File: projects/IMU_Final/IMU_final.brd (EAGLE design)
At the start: 54.6 x 22.5 mm, 6 parts, among them IC1 ISM330DHCXTR, J1 19428-0004

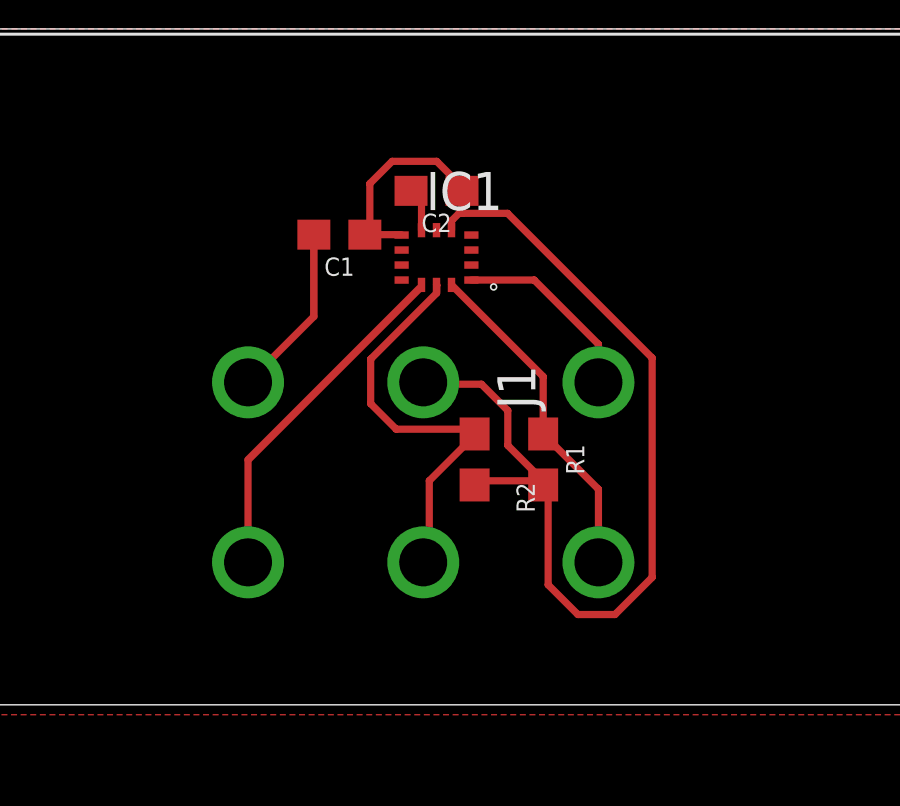
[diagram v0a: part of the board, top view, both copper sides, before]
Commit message: Final IMU Schematic
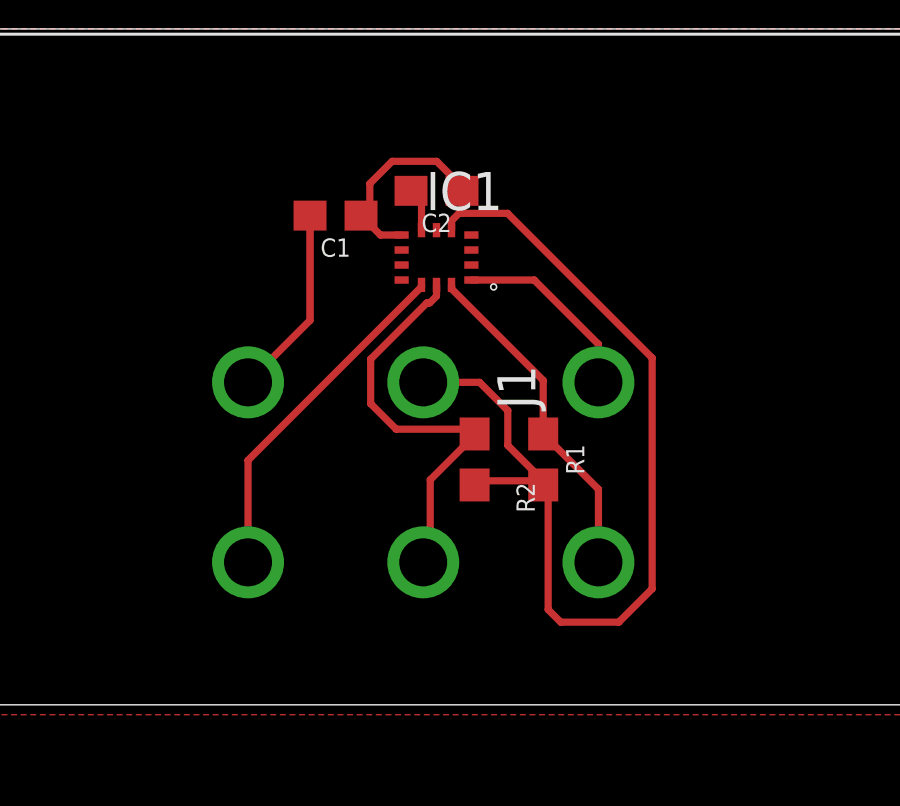
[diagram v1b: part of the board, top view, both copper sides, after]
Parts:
- moved C1 0.65 mm to (-1.14, 21.7)
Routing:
- net 3V3: track 40.1 -> 41.1 mm
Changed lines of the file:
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@@
 </autorouter>
 <elements>
-<element name="C1" library="SparkFun-Capacitors" package="0603" value="0.1uF" x="-1.016" y="21.082" smashed="yes" rot="R180">
-<attribute name="NAME" x="-1.016" y="20.32" size="0.6096" layer="25" font="vector" ratio="20" rot="R180" align="bottom-center"/>
-<attribute name="PROD_ID" value="CAP-00810" x="-16.256" y="56.642" size="1.778" layer="27" rot="R180" display="off"/>
-<attribute name="VALUE" x="-1.016" y="21.844" size="0.6096" layer="27" font="vector" ratio="20" rot="R180" align="top-center"/>
+<element name="C1" library="SparkFun-Capacitors" package="0603" value="0.1uF" x="-1.143" y="21.717" smashed="yes" rot="R180">
+<attribute name="NAME" x="-1.143" y="20.955" size="0.6096" layer="25" font="vector" ratio="20" rot="R180" align="bottom-center"/>
+<attribute name="PROD_ID" value="CAP-00810" x="-16.383" y="57.277" size="1.778" layer="27" rot="R180" display="off"/>
+<attribute name="VALUE" x="-1.143" y="22.479" size="0.6096" layer="27" font="vector" ratio="20" rot="R180" align="top-center"/>
 </element>
 <element name="C2" library="SparkFun-Capacitors" package="0603" value="0.1uF" x="2.2225" y="22.5425" smashed="yes" rot="R180">
@@
 <contactref element="IC1" pad="14"/>
 <contactref element="R1" pad="1"/>
-<wire x1="2.7225" y1="19.4075" x2="5.7785" y2="16.3515" width="0.2413" layer="1"/>
-<wire x1="5.7785" y1="16.3515" x2="5.7785" y2="14.439" width="0.2413" layer="1"/>
+<wire x1="5.7785" y1="16.2245" x2="2.7225" y2="19.2805" width="0.2413" layer="1"/>
+<wire x1="2.7225" y1="19.4075" x2="2.7225" y2="19.2805" width="0.2413" layer="1"/>
+<wire x1="5.7785" y1="16.2245" x2="5.7785" y2="14.439" width="0.2413" layer="1"/>
 <wire x1="5.7785" y1="14.439" x2="7.62" y2="12.5975" width="0.2413" layer="1"/>
 <wire x1="7.62" y1="12.5975" x2="7.62" y2="10.16" width="0.2413" layer="1"/>
@@
 <contactref element="J1" pad="3"/>
 <contactref element="IC1" pad="12"/>
-<wire x1="-4.06" y1="13.575625" x2="-4.06" y2="10.16" width="0.2413" layer="1"/>
-<wire x1="1.65945" y1="19.295075" x2="-4.06" y2="13.575625" width="0.254" layer="1"/>
-<wire x1="1.65945" y1="19.295075" x2="1.7225" y2="19.4075" width="0" layer="19" extent="1-1"/>
+<wire x1="1.7225" y1="19.4075" x2="1.7225" y2="19.344" width="0.2413" layer="1"/>
+<wire x1="1.7225" y1="19.344" x2="-4.06" y2="13.5615" width="0.2413" layer="1"/>
+<wire x1="-4.06" y1="13.5615" x2="-4.06" y2="10.16" width="0.2413" layer="1"/>
 </signal>
 <signal name="GND">
@@
 <wire x1="1.3725" y1="22.5425" x2="1.7225" y2="22.1925" width="0.2413" layer="1"/>
 <wire x1="1.7225" y1="22.1925" x2="1.7225" y2="21.2325" width="0.2413" layer="1"/>
-<wire x1="-1.727875" y1="21.082" x2="-1.866" y2="21.082" width="0.2413" layer="1"/>
-<wire x1="-1.866" y1="21.082" x2="-1.866" y2="18.354" width="0.254" layer="1"/>
-<wire x1="-1.866" y1="18.354" x2="-4.06" y2="16.16" width="0.2413" layer="1"/>
-<wire x1="1.06" y1="20.57" x2="-1.727875" y2="21.082" width="0" layer="19" extent="1-1"/>
+<wire x1="-1.993" y1="21.717" x2="-1.993" y2="18.227" width="0.254" layer="1"/>
+<wire x1="-1.993" y1="18.227" x2="-4.06" y2="16.16" width="0.2413" layer="1"/>
 </signal>
 <signal name="3V3">
@@
 <contactref element="C2" pad="1"/>
 <wire x1="3.0725" y1="22.5425" x2="3.0725" y2="21.7932" width="0.2413" layer="1"/>
-<wire x1="-0.166" y1="21.082" x2="1.048" y2="21.082" width="0.2413" layer="1"/>
-<wire x1="0" y1="22.7838" x2="0" y2="21.2979" width="0.2413" layer="1"/>
+<wire x1="0" y1="22.7838" x2="0" y2="22.098075" width="0.2413" layer="1"/>
 <wire x1="0.74295" y1="23.52675" x2="0" y2="22.7838" width="0.2413" layer="1"/>
 <wire x1="2.22885" y1="23.52675" x2="0.74295" y2="23.52675" width="0.2413" layer="1"/>
 <wire x1="2.9718" y1="22.7838" x2="2.22885" y2="23.52675" width="0.2413" layer="1"/>
-<wire x1="0" y1="21.2979" x2="-0.166" y2="21.082" width="0.2413" layer="1"/>
+<wire x1="0" y1="22.098075" x2="-0.293" y2="21.717" width="0.2413" layer="1"/>
 <wire x1="2.9718" y1="22.7838" x2="3.0725" y2="22.5425" width="0.2413" layer="1"/>
 <wire x1="5.69595" y1="12.8778" x2="3.71475" y2="12.8778" width="0.2413" layer="1"/>
 <wire x1="3.71475" y1="12.8778" x2="3.4925" y2="12.739" width="0.2413" layer="1"/>
 <wire x1="5.69595" y1="12.8778" x2="5.7785" y2="12.739" width="0.2413" layer="1"/>
-<wire x1="3.7211" y1="16.09725" x2="4.59905" y2="15.2193" width="0.2413" layer="1"/>
-<wire x1="1.9812" y1="16.09725" x2="3.7211" y2="16.09725" width="0.2413" layer="1"/>
 <wire x1="4.59105" y1="21.7932" x2="3.0725" y2="21.7932" width="0.2413" layer="1"/>
 <wire x1="9.4107" y1="16.97355" x2="4.59105" y2="21.7932" width="0.2413" layer="1"/>
-<wire x1="9.4107" y1="9.65835" x2="9.4107" y2="16.97355" width="0.2413" layer="1"/>
-<wire x1="8.17245" y1="8.4201" x2="9.4107" y2="9.65835" width="0.2413" layer="1"/>
-<wire x1="6.9342" y1="8.4201" x2="8.17245" y2="8.4201" width="0.2413" layer="1"/>
-<wire x1="5.9436" y1="9.4107" x2="6.9342" y2="8.4201" width="0.2413" layer="1"/>
-<wire x1="5.9436" y1="12.63015" x2="5.9436" y2="9.4107" width="0.2413" layer="1"/>
+<wire x1="9.4107" y1="9.27735" x2="9.4107" y2="16.97355" width="0.2413" layer="1"/>
+<wire x1="8.29945" y1="8.1661" x2="9.4107" y2="9.27735" width="0.2413" layer="1"/>
+<wire x1="6.3627" y1="8.1661" x2="8.29945" y2="8.1661" width="0.2413" layer="1"/>
+<wire x1="5.9436" y1="8.5852" x2="6.3627" y2="8.1661" width="0.2413" layer="1"/>
+<wire x1="5.9436" y1="12.63015" x2="5.9436" y2="8.5852" width="0.2413" layer="1"/>
 <wire x1="3.0725" y1="21.7932" x2="2.9718" y2="21.7932" width="0.2413" layer="1"/>
 <wire x1="5.9436" y1="12.63015" x2="5.7785" y2="12.739" width="0.2413" layer="1"/>
-<wire x1="4.59905" y1="15.2193" x2="4.59905" y2="14.056575" width="0.2413" layer="1"/>
+<wire x1="4.59905" y1="14.056575" x2="4.59905" y2="15.2193" width="0.2413" layer="1"/>
 <wire x1="5.7785" y1="12.877125" x2="5.7785" y2="12.739" width="0.2413" layer="1"/>
 <wire x1="4.59905" y1="14.056575" x2="5.7785" y2="12.877125" width="0.2413" layer="1"/>
 <wire x1="2.9718" y1="21.7932" x2="2.7225" y2="21.5439" width="0.2413" layer="1"/>
 <wire x1="2.7225" y1="21.5439" x2="2.7225" y2="21.2325" width="0.2413" layer="1"/>
-<wire x1="1.048" y1="21.082" x2="1.06" y2="21.07" width="0" layer="19" extent="1-1"/>
-<wire x1="1.78" y1="16.16" x2="1.9812" y2="16.09725" width="0" layer="19" extent="1-1"/>
+<wire x1="-0.293" y1="21.717" x2="0.354" y2="21.07" width="0.2413" layer="1"/>
+<wire x1="0.354" y1="21.07" x2="1.06" y2="21.07" width="0.2413" layer="1"/>
+<wire x1="3.65835" y1="16.16" x2="1.78" y2="16.16" width="0.2413" layer="1"/>
+<wire x1="4.59905" y1="15.2193" x2="3.65835" y2="16.16" width="0.2413" layer="1"/>
 </signal>
 <signal name="SDO">
@@
 <contactref element="IC1" pad="13"/>
 <contactref element="R2" pad="1"/>
-<wire x1="2.2225" y1="19.4075" x2="2.2272" y2="19.4028" width="0.2413" layer="1"/>
-<wire x1="2.2225" y1="19.4075" x2="2.23555" y2="19.39445" width="0.2413" layer="1"/>
-<wire x1="1.9812" y1="12.8778" x2="3.4671" y2="14.3637" width="0.2413" layer="1"/>
-<wire x1="1.9812" y1="10.4013" x2="1.9812" y2="12.8778" width="0.2413" layer="1"/>
+<wire x1="2.01295" y1="12.90955" x2="3.4671" y2="14.3637" width="0.2413" layer="1"/>
 <wire x1="3.4671" y1="14.3637" x2="3.4925" y2="14.439" width="0.2413" layer="1"/>
 <wire x1="0.02755" y1="15.44951875" x2="0.87901875" y2="14.59805" width="0.2413" layer="1"/>
 <wire x1="3.4925" y1="14.439" x2="3.33345" y2="14.59805" width="0.2413" layer="1"/>
 <wire x1="3.33345" y1="14.59805" x2="0.87901875" y2="14.59805" width="0.2413" layer="1"/>
-<wire x1="2.2272" y1="19.39445" x2="2.2272" y2="19.13363125" width="0.2413" layer="1"/>
-<wire x1="2.2272" y1="19.13363125" x2="0.02755" y2="16.93398125" width="0.2413" layer="1"/>
 <wire x1="0.02755" y1="16.93398125" x2="0.02755" y2="15.44951875" width="0.2413" layer="1"/>
-<wire x1="2.2272" y1="19.39445" x2="2.2225" y2="19.4075" width="0" layer="19" extent="1-1"/>
-<wire x1="1.78" y1="10.16" x2="1.9812" y2="10.4013" width="0" layer="19" extent="1-1"/>
+<wire x1="2.01295" y1="12.90955" x2="2.01295" y2="10.39295" width="0.2413" layer="1"/>
+<wire x1="2.01295" y1="10.39295" x2="1.78" y2="10.16" width="0.2413" layer="1"/>
+<wire x1="1.997425" y1="18.80805" x2="1.90161875" y2="18.80805" width="0.2413" layer="1"/>
+<wire x1="1.90161875" y1="18.80805" x2="0.02755" y2="16.93398125" width="0.2413" layer="1"/>
+<wire x1="2.2225" y1="19.4075" x2="2.2225" y2="19.033125" width="0.2413" layer="1"/>
+<wire x1="2.2225" y1="19.033125" x2="1.997425" y2="18.80805" width="0.2413" layer="1"/>
 </signal>
 <signal name="NC2">
